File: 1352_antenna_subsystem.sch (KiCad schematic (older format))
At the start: 27 parts, among them U201 cc1352p, U202 XMSSJJ3G0PA-054

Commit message: Moved MCU to its own sheet.
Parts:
- removed U201: cc1352p, Package_DFN_QFN:VQFN-48-1EP_7x7mm_P0.5mm_EP5.15x5.15mm, symbol cc1352:cc1352p
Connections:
- net labels removed: ZNP_BTN_1, ZNP_BTN_2, ZNP_LED_1, ZNP_LED_2, ZNP_RX, ZNP_TX
- wire segments 98 -> 81
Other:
- moved on the sheet: AE201, C202, C203, C205, C206, C207, C208, C209, C210, C212, L201, L202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

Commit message: Finished Adding MCU connections and combined crystal and MCU sheets.
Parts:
- removed AE202: 50Ω, Connector_Coaxial:U.FL_Hirose_U.FL-R-SMT-1_Vertical, symbol BeagleBone-Black-Cape-rescue:Antenna-Device
- removed C211: 100pF, Capacitor_SMD:C_0805_2012Metric_Pad1.18x1.45mm_HandSolder, symbol BeagleBone-Black-Cape-rescue:C-Device
- removed U202: XMSSJJ3G0PA-054, symbol cc1352:XMSSJJ3G0PA-054
- added C?: 47pF, Capacitor_SMD:C_0805_2012Metric_Pad1.18x1.45mm_HandSolder, symbol BeagleBone-Black-Cape-rescue:C-Device
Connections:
- net labels removed: PSU_3V3Out+, SPDT_CTL
- wire segments 81 -> 67
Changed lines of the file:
@@
 $Descr A4 11693 8268
 encoding utf-8
-Sheet 2 7
+Sheet 2 6
 Title ""
 Date ""
@@
 	3700 3350 3800 3350
 $Comp
-L cc1352:XMSSJJ3G0PA-054 U202
-U 1 1 61582047
-P 7000 -1800
-F 0 "U202" H 7000 -635 50  0000 C CNN
-F 1 "XMSSJJ3G0PA-054" H 7000 -726 50  0000 C CNN
-F 2 "" H 6988 -1897 50  0001 C CNN
-F 3 "" H 6988 -1897 50  0001 C CNN
-	1    7000 -1800
-	1    0    0    -1
-$EndComp
-Wire Wire Line
-	3000 -2200 4600 -2200
-Wire Wire Line
-	4600 -2200 4600 -1100
-Wire Wire Line
-	4600 -1100 5900 -1100
-Wire Wire Line
-	5900 -1700 5550 -1700
-Wire Wire Line
-	5550 -1700 5550 -1600
-Wire Wire Line
-	8100 -1100 8600 -1100
-Text GLabel 8500 -2400 2    50   Input ~ 0
-SPDT_CTL
-Wire Wire Line
-	8100 -2400 8500 -2400
-$Comp
 L BeagleBone-Black-Cape-rescue:C-Device C204
 U 1 1 615A901D
@@
 Wire Wire Line
 	4800 2300 5800 2300
-Wire Wire Line
-	4300 -1600 5000 -1600
-Wire Wire Line
-	5000 -2400 5000 -1600
-Wire Wire Line
-	5000 -2400 5900 -2400
-$Comp
-L power:GND #PWR0209
-U 1 1 615C0254
-P 5550 -1600
-F 0 "#PWR0209" H 5550 -1850 50  0001 C CNN
-F 1 "GND" H 5555 -1773 50  0000 C CNN
-F 2 "" H 5550 -1600 50  0001 C CNN
-F 3 "" H 5550 -1600 50  0001 C CNN
-	1    5550 -1600
-	1    0    0    -1
-$EndComp
-Text GLabel 8600 -1100 2    50   Input ~ 0
-PSU_3V3Out+
-$Comp
-L BeagleBone-Black-Cape-rescue:Antenna-Device AE202
-U 1 1 615CC691
-P 7150 -450
-F 0 "AE202" H 7230 -461 50  0000 L CNN
-F 1 "50Ω" H 7230 -552 50  0000 L CNN
-F 2 "Connector_Coaxial:U.FL_Hirose_U.FL-R-SMT-1_Vertical" H 7150 -450 50  0001 C CNN
-F 3 "~" H 7150 -450 50  0001 C CNN
-	1    7150 -450
-	1    0    0    -1
-$EndComp
-$Comp
-L BeagleBone-Black-Cape-rescue:C-Device C211
-U 1 1 615D7861
-P 7700 -250
-F 0 "C211" V 7448 -250 50  0000 C CNN
-F 1 "100pF" V 7539 -250 50  0000 C CNN
-F 2 "Capacitor_SMD:C_0805_2012Metric_Pad1.18x1.45mm_HandSolder" H 7738 -400 50  0001 C CNN
-F 3 "~" H 7700 -250 50  0001 C CNN
-	1    7700 -250
-	0    1    1    0
-$EndComp
-Wire Wire Line
-	7550 -250 7150 -250
 $Comp
 L power:GND #PWR0205
@@
 	1    0    0    -1
 $EndComp
-Wire Wire Line
-	7850 -250 9300 -250
-Wire Wire Line
-	9300 -1700 9300 -250
-Wire Wire Line
-	8100 -1700 9300 -1700
 $Comp
 L UserMade-BB-Zigbee-Gateway-CAPE:SKY13317-373 TF202
@@
 	5850 1700 5850 1550
 Wire Wire Line
-	5850 1550 8250 1550
-Wire Wire Line
 	6100 2300 7050 2300
 Wire Wire Line
@@
 	8750 5100 8750 5050
 Connection ~ 8350 5100
+$Comp
+L BeagleBone-Black-Cape-rescue:C-Device C?
+U 1 1 614F2671
+P 6000 1550
+F 0 "C?" V 5748 1550 50  0000 C CNN
+F 1 "47pF" V 5839 1550 50  0000 C CNN
+F 2 "Capacitor_SMD:C_0805_2012Metric_Pad1.18x1.45mm_HandSolder" H 6038 1400 50  0001 C CNN
+F 3 "~" H 6000 1550 50  0001 C CNN
+	1    6000 1550
+	0    1    1    0
+$EndComp
+Wire Wire Line
+	6150 1550 8250 1550
 $EndSCHEMATC

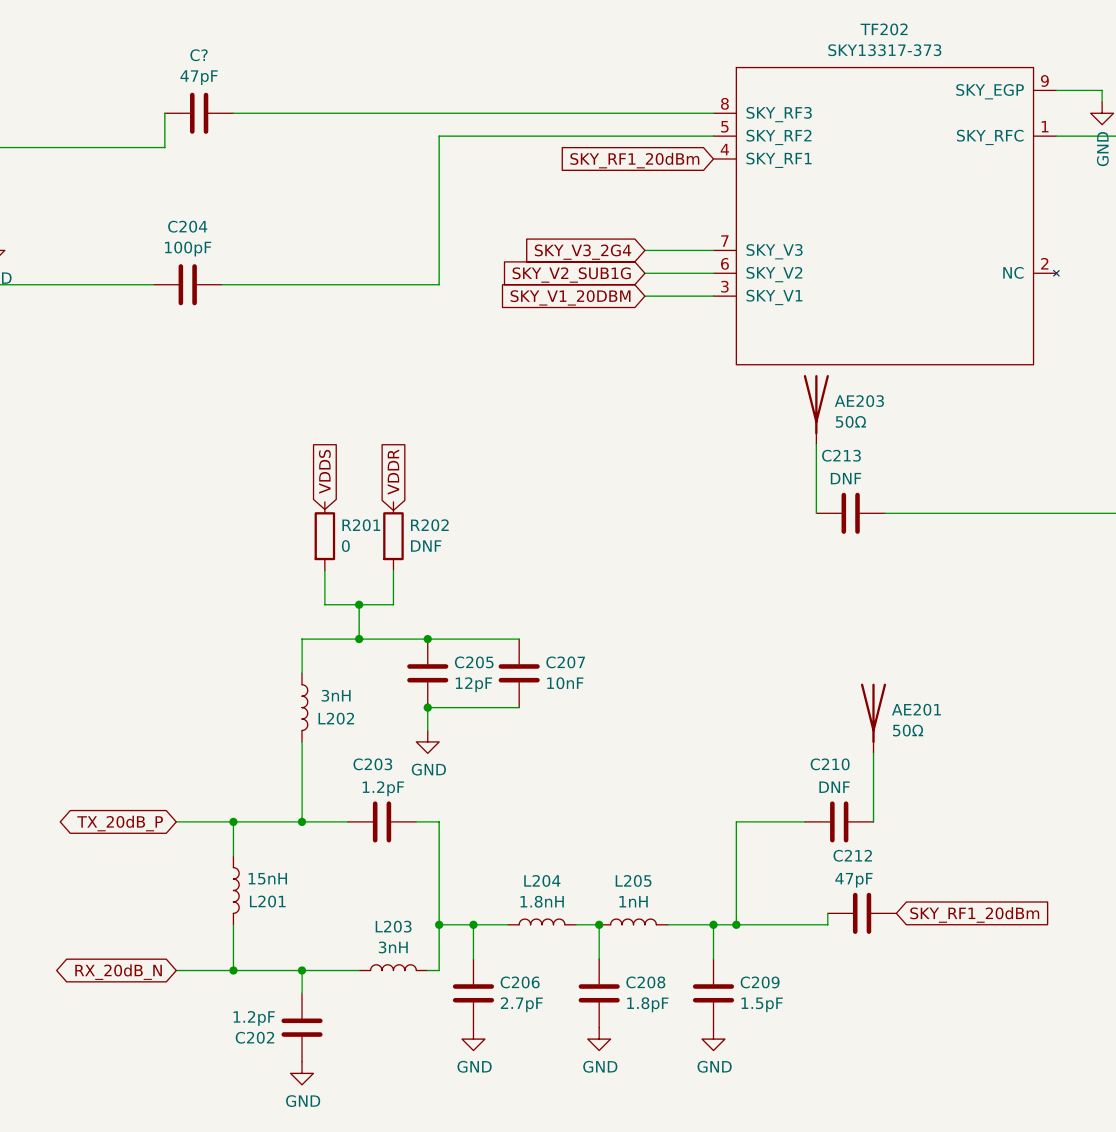
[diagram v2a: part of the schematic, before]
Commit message: part way through PCB rework using new components. 62 unconnected.
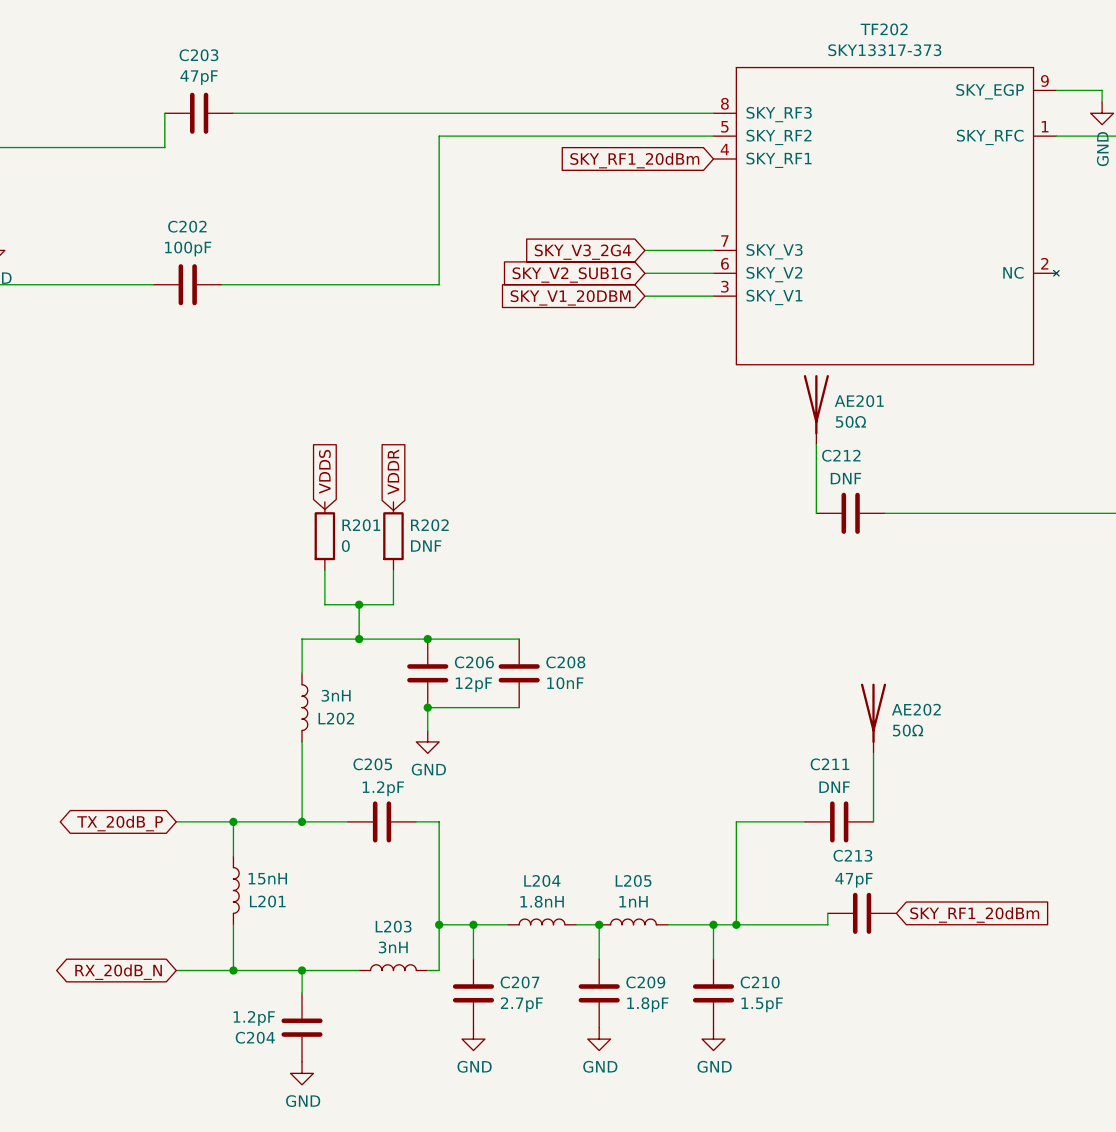
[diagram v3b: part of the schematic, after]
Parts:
- gave numbers to parts that had none: 1
- renumbered AE203 to AE201, AE201 to AE202, C204 to C202, C202 to C204, C203 to C205, C205 to C206, C206 to C207, C207 to C208, C208 to C209, C209 to C210, C210 to C211, C213 to C212, C212 to C213
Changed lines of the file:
@@
 	6450 5300 6450 5400
 $Comp
-L BeagleBone-Black-Cape-rescue:C-Device C202
+L BeagleBone-Black-Cape-rescue:C-Device C204
 U 1 1 605E8A57
 P 6450 5550
-F 0 "C202" H 6565 5596 50  0000 L CNN
+F 0 "C204" H 6565 5596 50  0000 L CNN
 F 1 "1.2pF" H 6565 5505 50  0000 L CNN
 F 2 "Capacitor_SMD:C_0805_2012Metric_Pad1.18x1.45mm_HandSolder" H 6488 5400 50  0001 C CNN
@@
 	7000 5300 7050 5300
 $Comp
-L BeagleBone-Black-Cape-rescue:C-Device C203
+L BeagleBone-Black-Cape-rescue:C-Device C205
 U 1 1 60611067
 P 6800 4650
-F 0 "C203" V 7050 4600 50  0000 L CNN
+F 0 "C205" V 7050 4600 50  0000 L CNN
 F 1 "1.2pF" V 6950 4550 50  0000 L CNN
 F 2 "Capacitor_SMD:C_0805_2012Metric_Pad1.18x1.45mm_HandSolder" H 6838 4500 50  0001 C CNN
@@
 	7050 5100 7050 5300
 $Comp
-L BeagleBone-Black-Cape-rescue:C-Device C205
+L BeagleBone-Black-Cape-rescue:C-Device C206
 U 1 1 60620B7F
 P 7000 4000
-F 0 "C205" H 7115 4046 50  0000 L CNN
+F 0 "C206" H 7115 4046 50  0000 L CNN
 F 1 "12pF" H 7115 3955 50  0000 L CNN
 F 2 "Capacitor_SMD:C_0805_2012Metric_Pad1.18x1.45mm_HandSolder" H 7038 3850 50  0001 C CNN
@@
 	7000 4150 7400 4150
 $Comp
-L BeagleBone-Black-Cape-rescue:C-Device C207
+L BeagleBone-Black-Cape-rescue:C-Device C208
 U 1 1 6062771A
 P 7400 4000
-F 0 "C207" H 7515 4046 50  0000 L CNN
+F 0 "C208" H 7515 4046 50  0000 L CNN
 F 1 "10nF" H 7515 3955 50  0000 L CNN
 F 2 "Capacitor_SMD:C_0805_2012Metric_Pad1.18x1.45mm_HandSolder" H 7438 3850 50  0001 C CNN
@@
 	7200 5100 7200 5250
 $Comp
-L BeagleBone-Black-Cape-rescue:C-Device C206
+L BeagleBone-Black-Cape-rescue:C-Device C207
 U 1 1 60632FC0
 P 7200 5400
-F 0 "C206" H 7315 5446 50  0000 L CNN
+F 0 "C207" H 7315 5446 50  0000 L CNN
 F 1 "2.7pF" H 7315 5355 50  0000 L CNN
 F 2 "Capacitor_SMD:C_0805_2012Metric_Pad1.18x1.45mm_HandSolder" H 7238 5250 50  0001 C CNN
@@
 	7650 5100 7750 5100
 $Comp
-L BeagleBone-Black-Cape-rescue:C-Device C208
+L BeagleBone-Black-Cape-rescue:C-Device C209
 U 1 1 60645553
 P 7750 5400
-F 0 "C208" H 7865 5446 50  0000 L CNN
+F 0 "C209" H 7865 5446 50  0000 L CNN
 F 1 "1.8pF" H 7865 5355 50  0000 L CNN
 F 2 "Capacitor_SMD:C_0805_2012Metric_Pad1.18x1.45mm_HandSolder" H 7788 5250 50  0001 C CNN
@@
 $EndComp
 $Comp
-L BeagleBone-Black-Cape-rescue:C-Device C209
+L BeagleBone-Black-Cape-rescue:C-Device C210
 U 1 1 60652D1E
 P 8250 5400
-F 0 "C209" H 8365 5446 50  0000 L CNN
+F 0 "C210" H 8365 5446 50  0000 L CNN
 F 1 "1.5pF" H 8365 5355 50  0000 L CNN
 F 2 "Capacitor_SMD:C_0805_2012Metric_Pad1.18x1.45mm_HandSolder" H 8288 5250 50  0001 C CNN
@@
 	8350 4650 8650 4650
 $Comp
-L BeagleBone-Black-Cape-rescue:C-Device C210
+L BeagleBone-Black-Cape-rescue:C-Device C211
 U 1 1 6066C58A
 P 8800 4650
-F 0 "C210" V 9050 4600 50  0000 L CNN
+F 0 "C211" V 9050 4600 50  0000 L CNN
 F 1 "DNF" V 8950 4600 50  0000 L CNN
 F 2 "Capacitor_SMD:C_0805_2012Metric_Pad1.18x1.45mm_HandSolder" H 8838 4500 50  0001 C CNN
@@
 $EndComp
 $Comp
-L BeagleBone-Black-Cape-rescue:Antenna-Device AE201
+L BeagleBone-Black-Cape-rescue:Antenna-Device AE202
 U 1 1 6066FAEC
 P 8950 4150
-F 0 "AE201" H 9030 4139 50  0000 L CNN
+F 0 "AE202" H 9030 4139 50  0000 L CNN
 F 1 "50Ω" H 9030 4048 50  0000 L CNN
 F 2 "Connector_Coaxial:U.FL_Hirose_U.FL-R-SMT-1_Vertical" H 8950 4150 50  0001 C CNN
@@
 	3700 3350 3800 3350
 $Comp
-L BeagleBone-Black-Cape-rescue:C-Device C204
+L BeagleBone-Black-Cape-rescue:C-Device C202
 U 1 1 615A901D
 P 5950 2300
-F 0 "C204" V 5698 2300 50  0000 C CNN
+F 0 "C202" V 5698 2300 50  0000 C CNN
 F 1 "100pF" V 5789 2300 50  0000 C CNN
 F 2 "Capacitor_SMD:C_0805_2012Metric_Pad1.18x1.45mm_HandSolder" H 5988 2150 50  0001 C CNN
@@
 	9950 1450 9950 1500
 $Comp
-L BeagleBone-Black-Cape-rescue:GND-power #PWR0114
+L BeagleBone-Black-Cape-rescue:GND-power #PWR0209
 U 1 1 61500151
 P 9950 1500
-F 0 "#PWR0114" H 9950 1250 50  0001 C CNN
+F 0 "#PWR0209" H 9950 1250 50  0001 C CNN
 F 1 "GND" V 9955 1372 50  0000 R CNN
 F 2 "" H 9950 1500 50  0001 C CNN
@@
 	10200 1650 10200 3300
 $Comp
-L BeagleBone-Black-Cape-rescue:C-Device C213
+L BeagleBone-Black-Cape-rescue:C-Device C212
 U 1 1 6150D584
 P 8850 3300
-F 0 "C213" V 9100 3250 50  0000 L CNN
+F 0 "C212" V 9100 3250 50  0000 L CNN
 F 1 "DNF" V 9000 3250 50  0000 L CNN
 F 2 "Capacitor_SMD:C_0805_2012Metric_Pad1.18x1.45mm_HandSolder" H 8888 3150 50  0001 C CNN
@@
 $EndComp
 $Comp
-L BeagleBone-Black-Cape-rescue:Antenna-Device AE203
+L BeagleBone-Black-Cape-rescue:Antenna-Device AE201
 U 1 1 615152E3
 P 8700 2800
-F 0 "AE203" H 8780 2789 50  0000 L CNN
+F 0 "AE201" H 8780 2789 50  0000 L CNN
 F 1 "50Ω" H 8780 2698 50  0000 L CNN
 F 2 "Connector_Coaxial:U.FL_Hirose_U.FL-R-SMT-1_Vertical" H 8700 2800 50  0001 C CNN
@@
 	8700 3300 8700 3000
 $Comp
-L BeagleBone-Black-Cape-rescue:C-Device C212
+L BeagleBone-Black-Cape-rescue:C-Device C213
 U 1 1 61536BA3
 P 8900 5050
-F 0 "C212" V 9150 5000 50  0000 L CNN
+F 0 "C213" V 9150 5000 50  0000 L CNN
 F 1 "47pF" V 9050 5000 50  0000 L CNN
 F 2 "Capacitor_SMD:C_0805_2012Metric_Pad1.18x1.45mm_HandSolder" H 8938 4900 50  0001 C CNN
@@
 Connection ~ 8350 5100
 $Comp
-L BeagleBone-Black-Cape-rescue:C-Device C?
+L BeagleBone-Black-Cape-rescue:C-Device C203
 U 1 1 614F2671
 P 6000 1550
-F 0 "C?" V 5748 1550 50  0000 C CNN
+F 0 "C203" V 5748 1550 50  0000 C CNN
 F 1 "47pF" V 5839 1550 50  0000 C CNN
 F 2 "Capacitor_SMD:C_0805_2012Metric_Pad1.18x1.45mm_HandSolder" H 6038 1400 50  0001 C CNN

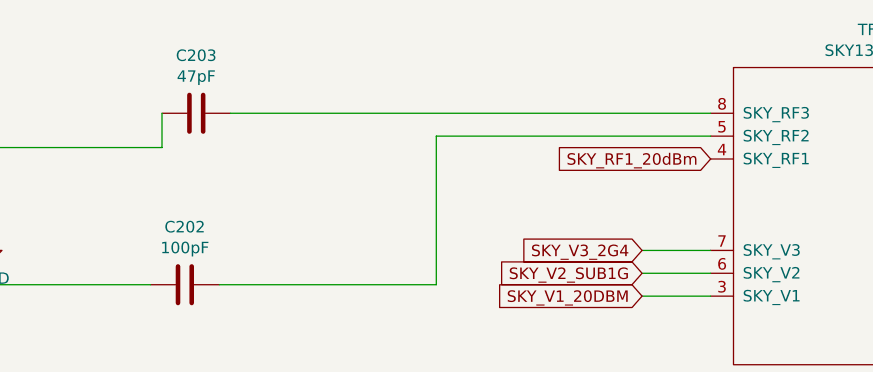
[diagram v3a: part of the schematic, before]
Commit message: finished RF side of schematic. We need ground planes and Xtals
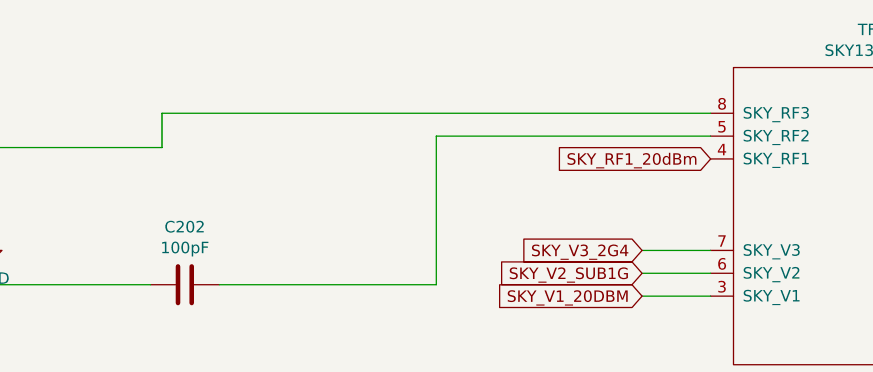
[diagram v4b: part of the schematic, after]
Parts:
- removed C203: 47pF, Capacitor_SMD:C_0805_2012Metric_Pad1.18x1.45mm_HandSolder, symbol BeagleBone-Black-Cape-rescue:C-Device
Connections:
- net at TF202.8 (SKY_RF3): now also TF201.1 (ANT_2.4GHz)
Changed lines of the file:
@@
 	8750 5100 8750 5050
 Connection ~ 8350 5100
-$Comp
-L BeagleBone-Black-Cape-rescue:C-Device C203
-U 1 1 614F2671
-P 6000 1550
-F 0 "C203" V 5748 1550 50  0000 C CNN
-F 1 "47pF" V 5839 1550 50  0000 C CNN
-F 2 "Capacitor_SMD:C_0805_2012Metric_Pad1.18x1.45mm_HandSolder" H 6038 1400 50  0001 C CNN
-F 3 "~" H 6000 1550 50  0001 C CNN
-	1    6000 1550
-	0    1    1    0
-$EndComp
 Wire Wire Line
-	6150 1550 8250 1550
+	5850 1550 8250 1550
 $EndSCHEMATC
